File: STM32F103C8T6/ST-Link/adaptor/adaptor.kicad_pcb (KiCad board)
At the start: 2 copper layers, 53 x 23 mm, 4 parts, among them J1 Conn_01x20_Socket, J2 Conn_01x20_Socket, J3 Conn_01x04_Pin

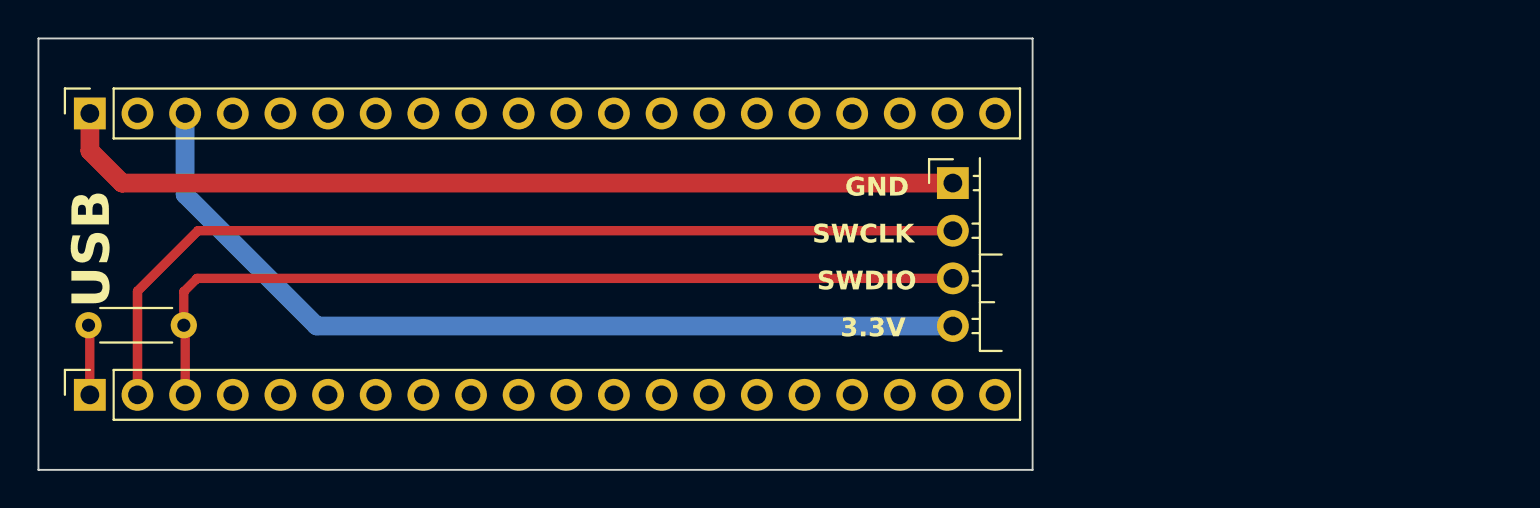
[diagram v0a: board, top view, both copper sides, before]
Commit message: SWD socket connector
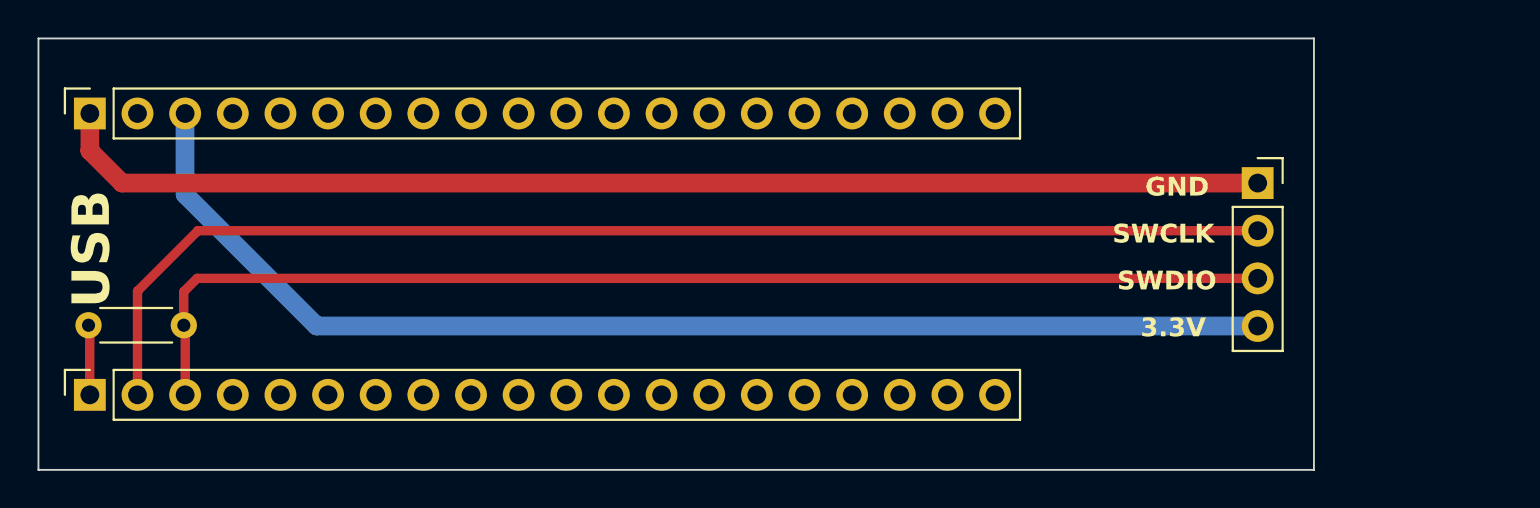
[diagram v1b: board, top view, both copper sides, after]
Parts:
- J3: footprint Connector_PinHeader_2.54mm:PinHeader_1x04_P2.54mm_Horizontal -> Connector_PinSocket_2.54mm:PinSocket_1x04_P2.54mm_Vertical
- moved J3 16.2 mm to (184.0, 67.7)
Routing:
- net /SWDIO: track 46.8 -> 63.1 mm
- net /SWCLK: track 50.3 -> 66.6 mm
- net /GND: track 48.7 -> 65.0 mm
- net /3.3V: track 48.2 -> 64.4 mm
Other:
- board size 53 x 23 mm -> 68 x 23 mm

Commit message: Space for SWD connector
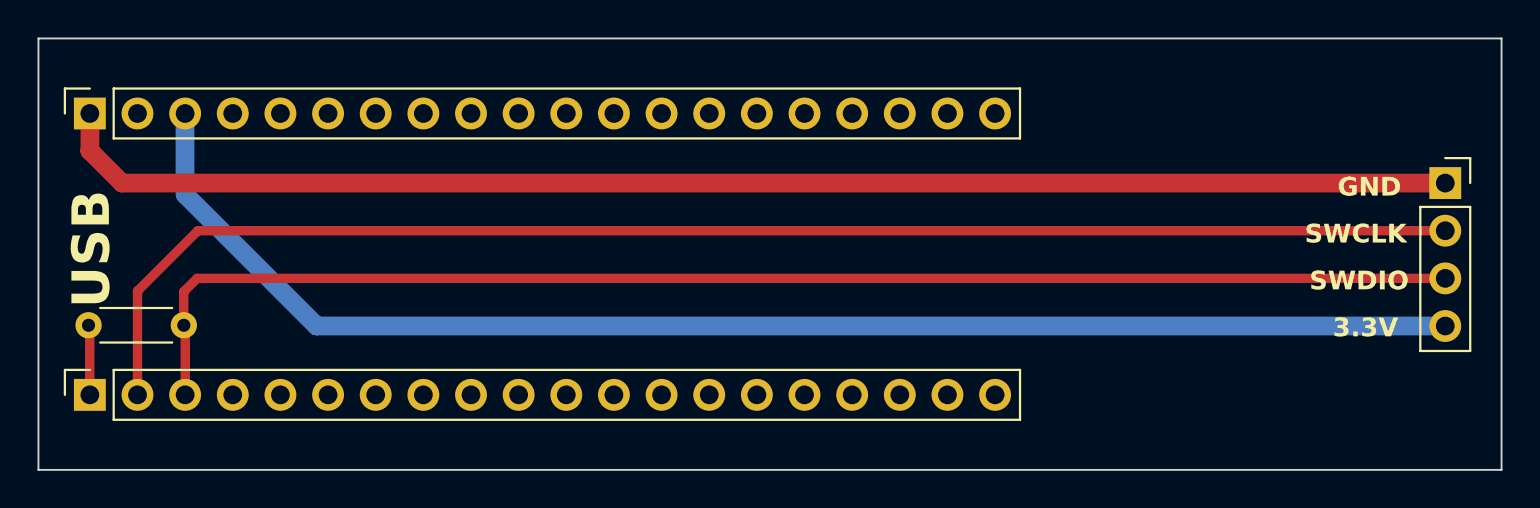
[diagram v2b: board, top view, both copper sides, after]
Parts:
- moved J3 10.0 mm to (194.0, 67.7)
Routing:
- net /SWCLK: track 66.6 -> 76.6 mm
- net /GND: track 65.0 -> 75.0 mm
- net /3.3V: track 64.4 -> 74.4 mm
- net /SWDIO: track 63.1 -> 73.1 mm
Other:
- board size 68 x 23 mm -> 78 x 23 mm
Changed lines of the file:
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@@
   )
   (footprint "Connector_PinSocket_2.54mm:PinSocket_1x04_P2.54mm_Vertical" (layer "F.Cu")
-    (at 184 67.71)
+    (at 194 67.71)
     (descr "Through hole straight socket strip, 1x04, 2.54mm pitch, single row (from Kicad 4.0.7), script generated")
     (tags "Through hole socket strip THT 1x04 2.54mm single row")
@@
   (gr_line (start 119 83) (end 119 60)
     (stroke (width 0.1) (type default)) (layer "Edge.Cuts"))
-  (gr_line (start 187 83) (end 119 83)
+  (gr_line (start 197 60) (end 119 60)
     (stroke (width 0.1) (type default)) (layer "Edge.Cuts"))
-  (gr_line (start 187 60) (end 119 60)
+  (gr_line (start 197 83) (end 119 83)
     (stroke (width 0.1) (type default)) (layer "Edge.Cuts"))
-  (gr_line (start 187 60) (end 187 83)
+  (gr_line (start 197 60) (end 197 83)
     (stroke (width 0.1) (type default)) (layer "Edge.Cuts"))
-  (gr_text "SWDIO" (at 182 73.5) (layer "B.SilkS")
+  (gr_text "SWDIO" (at 192 73.5) (layer "B.SilkS")
     (effects (font (size 1 1) (thickness 0.2) bold) (justify left bottom mirror))
   )
-  (gr_text "3.3V" (at 182 76) (layer "B.SilkS")
+  (gr_text "3.3V" (at 192 76) (layer "B.SilkS")
     (effects (font (size 1 1) (thickness 0.2) bold) (justify left bottom mirror))
   )
-  (gr_text "GND" (at 182 68.25) (layer "B.SilkS")
+  (gr_text "GND" (at 192 68.25) (layer "B.SilkS")
     (effects (font (size 1 1) (thickness 0.2) bold) (justify left bottom mirror))
   )
@@
     (effects (font (size 2 2) (thickness 0.2) bold) (justify left bottom mirror))
   )
-  (gr_text "SWCLK" (at 182 71) (layer "B.SilkS")
+  (gr_text "SWCLK" (at 192 71) (layer "B.SilkS")
     (effects (font (size 1 1) (thickness 0.2) bold) (justify left bottom mirror))
   )
-  (gr_text "SWDIO" (at 176.5 73.5) (layer "F.SilkS")
+  (gr_text "SWDIO" (at 186.75 73.5) (layer "F.SilkS")
     (effects (font (size 1 1) (thickness 0.2) bold) (justify left bottom))
   )
-  (gr_text "GND" (at 178 68.5) (layer "F.SilkS")
+  (gr_text "GND" (at 188.25 68.5) (layer "F.SilkS")
     (effects (font (size 1 1) (thickness 0.2) bold) (justify left bottom))
   )
-  (gr_text "SWCLK" (at 176.25 71) (layer "F.SilkS")
+  (gr_text "SWCLK" (at 186.5 71) (layer "F.SilkS")
     (effects (font (size 1 1) (thickness 0.2) bold) (justify left bottom))
   )
-  (gr_text "3.3V" (at 177.75 76) (layer "F.SilkS")
+  (gr_text "3.3V" (at 188 76) (layer "F.SilkS")
     (effects (font (size 1 1) (thickness 0.2) bold) (justify left bottom))
   )
@@
   (segment (start 121.74 75.36) (end 121.67 75.29) (width 0.5) (layer "F.Cu") (net 1))
   (segment (start 124.28 73.47) (end 127.5 70.25) (width 0.5) (layer "F.Cu") (net 2))
-  (segment (start 127.5 70.25) (end 184 70.25) (width 0.5) (layer "F.Cu") (net 2))
+  (segment (start 127.5 70.25) (end 194 70.25) (width 0.5) (layer "F.Cu") (net 2))
   (segment (start 124.28 79) (end 124.28 73.47) (width 0.5) (layer "F.Cu") (net 2))
-  (segment (start 127.46 72.79) (end 184 72.79) (width 0.5) (layer "F.Cu") (net 3))
+  (segment (start 126.75 75.29) (end 126.75 73.5) (width 0.5) (layer "F.Cu") (net 3))
   (segment (start 126.82 75.36) (end 126.75 75.29) (width 0.5) (layer "F.Cu") (net 3))
+  (segment (start 126.82 79) (end 126.82 75.36) (width 0.5) (layer "F.Cu") (net 3))
+  (segment (start 127.46 72.79) (end 194 72.79) (width 0.5) (layer "F.Cu") (net 3))
   (segment (start 126.75 73.5) (end 127.46 72.79) (width 0.5) (layer "F.Cu") (net 3))
-  (segment (start 126.82 79) (end 126.82 75.36) (width 0.5) (layer "F.Cu") (net 3))
-  (segment (start 126.75 75.29) (end 126.75 73.5) (width 0.5) (layer "F.Cu") (net 3))
-  (segment (start 123.46 67.71) (end 184 67.71) (width 1) (layer "F.Cu") (net 21))
+  (segment (start 123.46 67.71) (end 194 67.71) (width 1) (layer "F.Cu") (net 21))
+  (segment (start 121.74 64) (end 121.74 65.99) (width 1) (layer "F.Cu") (net 21))
   (segment (start 121.74 65.99) (end 123.46 67.71) (width 1) (layer "F.Cu") (net 21))
-  (segment (start 121.74 64) (end 121.74 65.99) (width 1) (layer "F.Cu") (net 21))
-  (segment (start 133.83 75.33) (end 184 75.33) (width 1) (layer "B.Cu") (net 23))
+  (segment (start 126.82 68.32) (end 133.83 75.33) (width 1) (layer "B.Cu") (net 23))
   (segment (start 126.82 64) (end 126.82 68.32) (width 1) (layer "B.Cu") (net 23))
-  (segment (start 126.82 68.32) (end 133.83 75.33) (width 1) (layer "B.Cu") (net 23))
+  (segment (start 133.83 75.33) (end 194 75.33) (width 1) (layer "B.Cu") (net 23))
 )
